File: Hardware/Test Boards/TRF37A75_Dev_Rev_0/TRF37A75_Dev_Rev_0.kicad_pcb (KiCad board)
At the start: 4 copper layers, 48 x 48 mm, 23 parts, among them J1 USB_B_Micro, J2 Conn_01x02, J3 SMA, J4 SMA, U1 TRF37A75

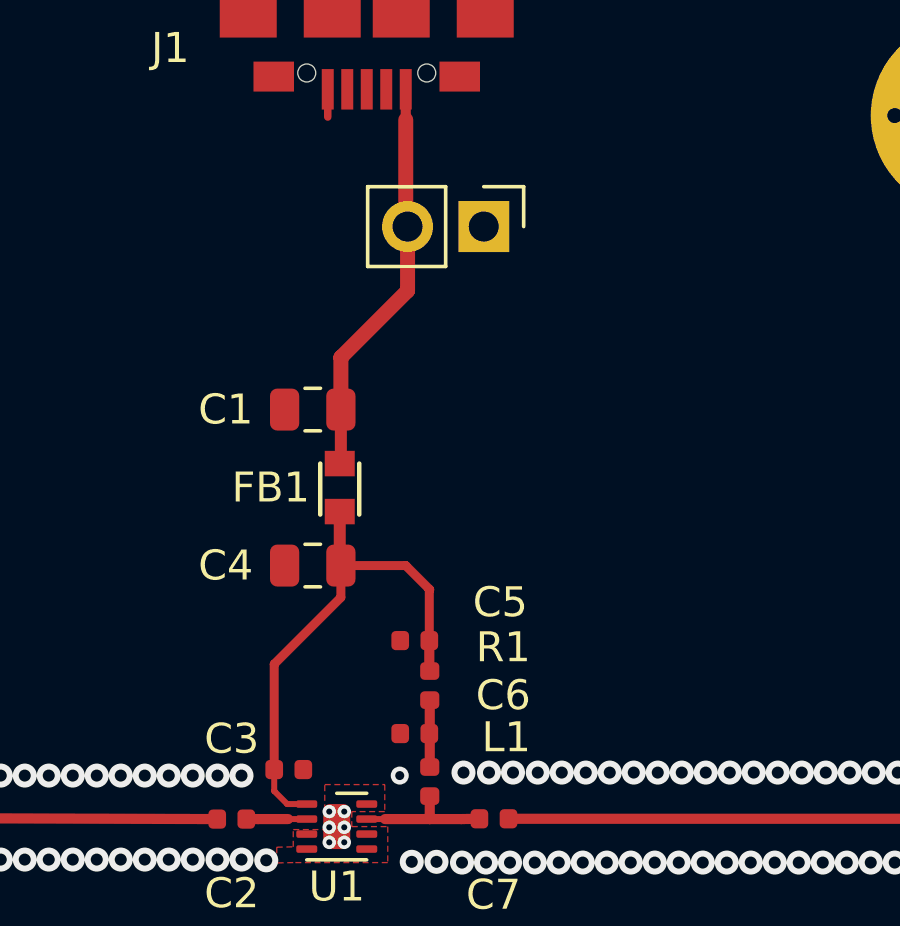
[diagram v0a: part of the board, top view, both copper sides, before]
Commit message: Started proper VNA schematic capture + new amp gerbers generated
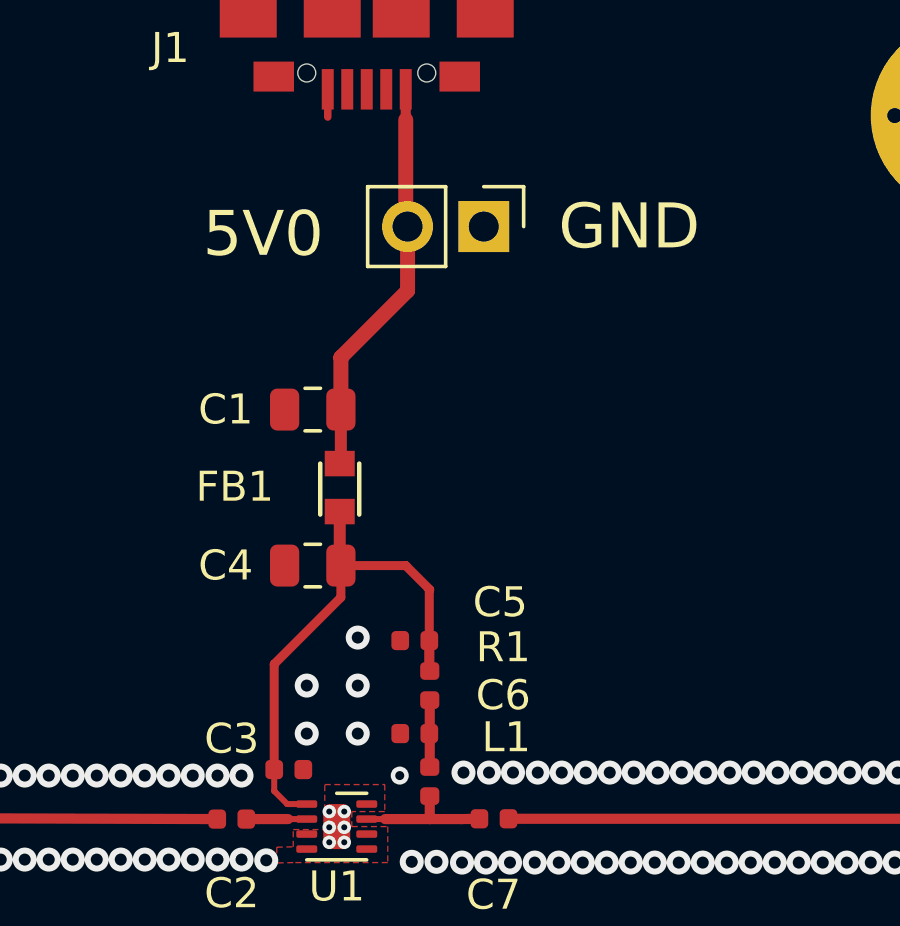
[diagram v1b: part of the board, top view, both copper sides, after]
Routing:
- net GND: vias 122 -> 127
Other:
- board text added: "5V0"
- board text added: "GND"
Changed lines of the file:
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@@
-(kicad_pcb (version 20171130) (host pcbnew "(5.0.2)-1")
+(kicad_pcb (version 20171130) (host pcbnew "(5.1.0)-1")
   (general
     (thickness 1.6)
-    (drawings 8)
-    (tracks 161)
+    (drawings 10)
+    (tracks 166)
     (zones 0)
     (modules 23)
@@
     (zone_45_only no)
     (trace_min 0.2)
-    (segment_width 0.2)
-    (edge_width 0.2)
     (via_size 0.8)
     (via_drill 0.4)
@@
     (uvia_min_size 0.2)
     (uvia_min_drill 0.1)
+    (edge_width 0.2)
+    (segment_width 0.2)
     (pcb_text_width 0.3)
     (pcb_text_size 1.5 1.5)
@@
     (visible_elements 7FFFFFFF)
     (pcbplotparams
-      (layerselection 0x010fc_ffffffff)
-      (usegerberextensions false)
+      (layerselection 0x010f8_ffffffff)
+      (usegerberextensions true)
       (usegerberattributes false)
       (usegerberadvancedattributes false)
@@
       (outputformat 1)
       (mirror false)
-      (drillshape 1)
+      (drillshape 0)
       (scaleselection 1)
       (outputdirectory ""))
@@
     (tags "Ferrite Bead")
     (attr smd)
-    (fp_text reference FB1 (at 0 -2.3 180) (layer F.SilkS)
+    (fp_text reference FB1 (at 0.025 -3.5 180) (layer F.SilkS)
       (effects (font (size 1 1) (thickness 0.15)))
     )
@@
       (effects (font (size 1 1) (thickness 0.15)) (justify mirror))
     )
+  )
+  (gr_text GND (at 128.75 68.7) (layer F.SilkS)
+    (effects (font (size 1.5 1.5) (thickness 0.3)))
+  )
+  (gr_text 5V0 (at 116.55 68.95) (layer F.SilkS)
+    (effects (font (size 1.5 1.5) (thickness 0.3)))
   )
   (gr_line (start 102 60) (end 140 60) (layer Edge.Cuts) (width 0.2))
@@
   (via (at 116.65 89.825) (size 0.8) (drill 0.4) (layers F.Cu B.Cu) (net 2))
   (segment (start 118.7 64.125) (end 118.7 65.05) (width 0.25) (layer F.Cu) (net 2))
+  (via (at 119.7 85.6) (size 0.8) (drill 0.4) (layers F.Cu B.Cu) (net 2))
+  (via (at 119.7 84) (size 0.8) (drill 0.4) (layers F.Cu B.Cu) (net 2))
+  (via (at 119.7 82.4) (size 0.8) (drill 0.4) (layers F.Cu B.Cu) (net 2))
+  (via (at 118 84) (size 0.8) (drill 0.4) (layers F.Cu B.Cu) (net 2))
+  (via (at 118 85.6) (size 0.8) (drill 0.4) (layers F.Cu B.Cu) (net 2))
   (segment (start 99 88.4) (end 103.94 88.4) (width 0.34) (layer F.Cu) (net 3))
   (segment (start 115.015 88.45) (end 99 88.4) (width 0.34) (layer F.Cu) (net 3))
@@
       )
     )
+  )
+  (zone (net 0) (net_name "") (layer In1.Cu) (hatch edge 0.508)
+    (connect_pads (clearance 0.4))
+    (min_thickness 0.254)
+    (keepout (tracks allowed) (vias allowed) (copperpour not_allowed))
+    (fill (arc_segments 16) (thermal_gap 0.508) (thermal_bridge_width 0.508))
+    (polygon
+      (pts
+        (xy 141.15 87.7) (xy 141.15 89.075) (xy 144.85 89.075) (xy 144.85 87.725)
+      )
+    )
+  )
+  (zone (net 0) (net_name "") (layer In1.Cu) (hatch edge 0.508)
+    (connect_pads (clearance 0.4))
+    (min_thickness 0.254)
+    (keepout (tracks allowed) (vias allowed) (copperpour not_allowed))
+    (fill (arc_segments 16) (thermal_gap 0.508) (thermal_bridge_width 0.508))
+    (polygon
+      (pts
+        (xy 97.15 87.7) (xy 97.15 89.075) (xy 100.85 89.075) (xy 100.85 87.725)
+      )
+    )
